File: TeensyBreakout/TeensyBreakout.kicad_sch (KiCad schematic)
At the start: 23 parts, among them J1 EncDriveRight, J10 MC3, J11 CurrSB, J12 UWB, J13 UVB Divider, J14 3.3V, J15 Relay, J2 EncDriveLeft, J3 EncExcavation, J4 Load Cell 1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

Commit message: Changes
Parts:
- removed J14: 3.3V, teensy:2pinJST, symbol Connector:Conn_01x02_Pin
- removed J4: Load Cell 1, teensy:2pinJST, symbol Connector:Conn_01x02_Pin
- removed J5: Load Cell 2, teensy:2pinJST, symbol Connector:Conn_01x02_Pin
- removed J6: GND, teensy:5pinJST, symbol Connector:Conn_01x05_Pin
- removed J7: 5V, teensy:3pinJST, symbol Connector:Conn_01x03_Pin
- added J4: Load Cell 2, teensy:4pinJST, symbol Connector:Conn_01x04_Pin
- added J5: Load Cell 1, teensy:4pinJST, symbol Connector:Conn_01x04_Pin
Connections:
- net +3.3V: now also J4.3 (Pin_3), J5.3 (Pin_3)
- net +5V: now also J1.2 (Pin_2), J2.2 (Pin_2), J3.2 (Pin_2)
- net GND: now also J1.4 (Pin_4), J2.4 (Pin_4), J3.4 (Pin_4), J4.4 (Pin_4), J5.4 (Pin_4)
- net WCLK1: now also J5.1 (Pin_1)
- net WCLK2: now also J4.1 (Pin_1)
- net WDAT1: now also J5.2 (Pin_2)
- net WDAT2: now also J4.2 (Pin_2)
- no-connect marks 51 -> 45

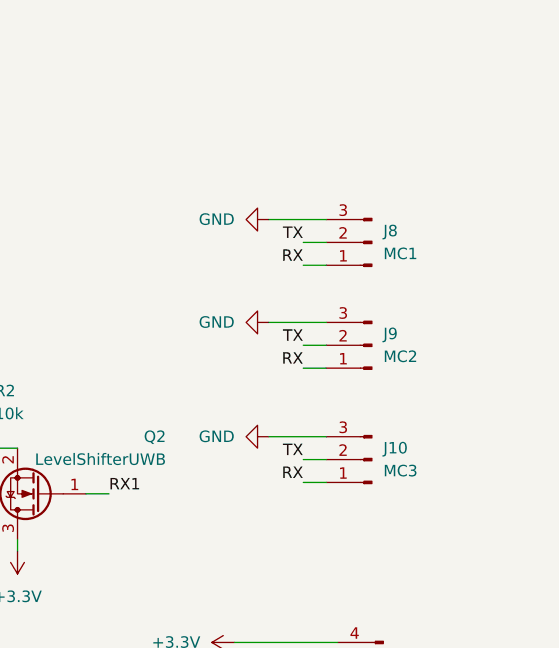
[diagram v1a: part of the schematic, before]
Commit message: added fuses to gnd input from MCs
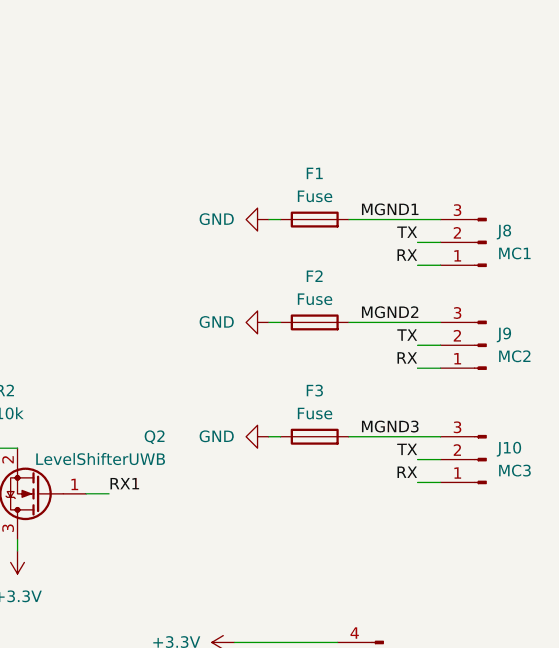
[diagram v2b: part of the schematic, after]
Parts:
- added F1, F2, F3: Fuse, Resistor_SMD:R_0603_1608Metric_Pad0.98x0.95mm_HandSolder, symbol Device:Fuse
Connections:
- net GND: now also F1.1, F2.1, F3.1; no longer J10.3 (Pin_3), J8.3 (Pin_3), J9.3 (Pin_3)
- new net MGND1: F1.2, J8.3 (Pin_3)
- new net MGND2: F2.2, J9.3 (Pin_3)
- new net MGND3: F3.2, J10.3 (Pin_3)
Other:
- moved on the sheet: J10, J8, J9

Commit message: minor changes
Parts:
- removed F2, F3: Fuse, Resistor_SMD:R_0603_1608Metric_Pad0.98x0.95mm_HandSolder, symbol Device:Fuse
- added R5: 0, Resistor_SMD:R_0805_2012Metric_Pad1.20x1.40mm_HandSolder, symbol Device:R_US
- added TP1: TestPoint, Connector_Pin:Pin_D0.9mm_L10.0mm_W2.4mm_FlatFork, symbol Connector:TestPoint
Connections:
- net MGND2 is gone; now on net MGND: J9.3 (Pin_3)
- net MGND3 is gone; now on net MGND: J10.3 (Pin_3)
- net +5V: now also R5.1, TP1.1; no longer U2.48 (VIN)
- net MGND1 renamed MGND
- new net 5V_Teensy: R5.2, U2.48 (VIN)
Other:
- moved on the sheet: F1
